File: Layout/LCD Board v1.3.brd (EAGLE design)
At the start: 37 parts, among them IC1 MAX3232CPE, IC2 MAX3232CPE, IC3 788TV, IC4 788TV

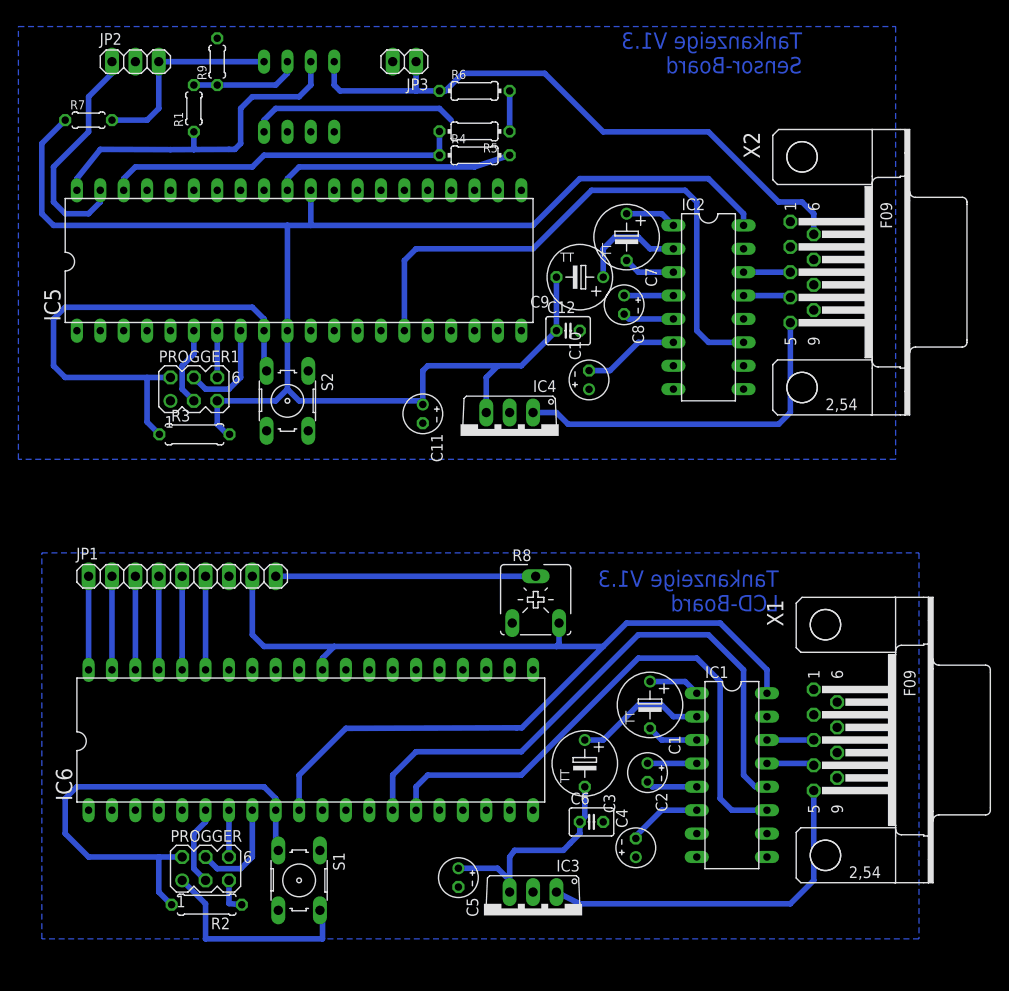
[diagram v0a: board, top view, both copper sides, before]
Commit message: Spannungsregler zu lm1117 und Input Cap hinzugefügt
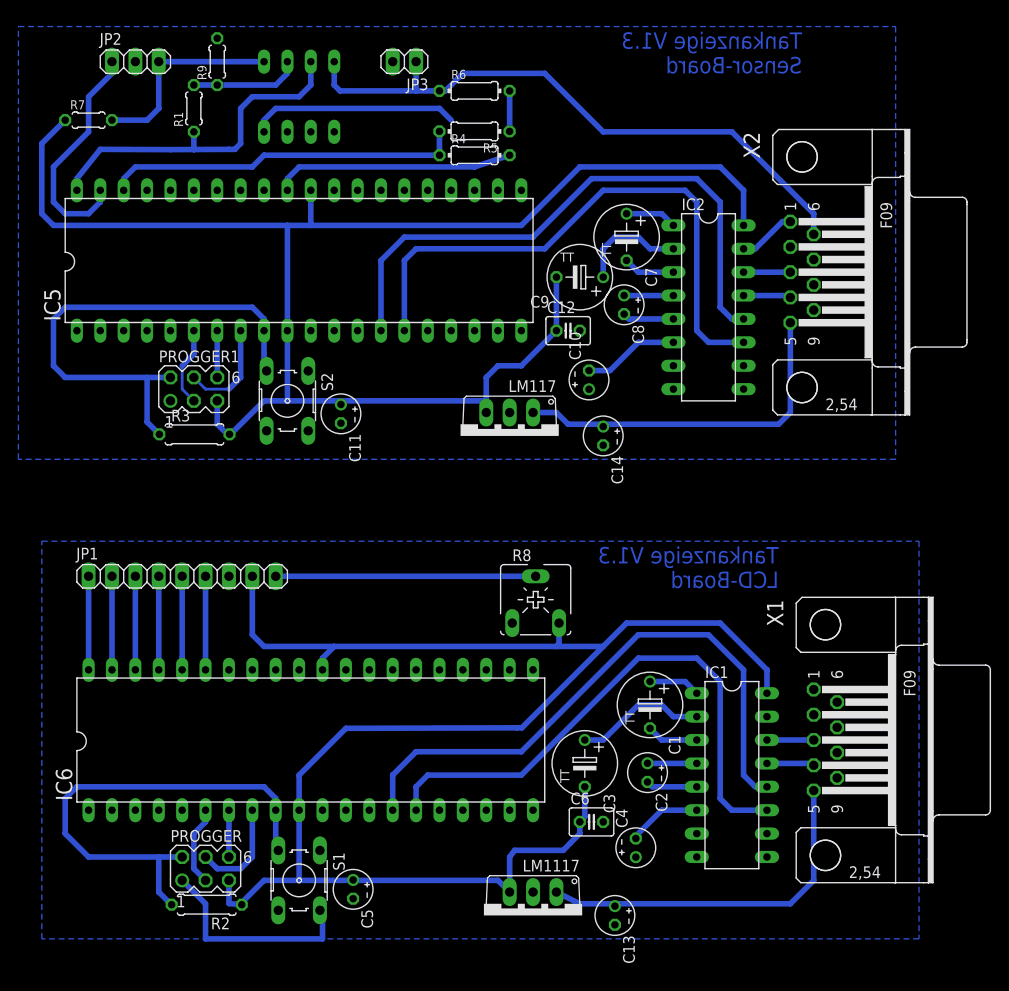
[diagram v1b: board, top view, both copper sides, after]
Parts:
- added C13, C14: 10uF, rcl:E2-4
- C11, C5: value 500uF -> 10uF
- moved C5 11.5 mm to (45.2, 6.65)
- moved C11 8.89 mm to (43.9, 58.3)
- renumbered IC3 to LM1117, IC4 to LM117
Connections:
- net +12V: now also C13.+, C14.+
- net GND: now also C13.-, C14.-
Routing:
- net N$33: track 0.00 -> 63.7 mm
- net VCC: track 318.4 -> 348.9 mm
- net GND: track 72.1 -> 78.4 mm
- net +12V: track 145.2 -> 145.7 mm

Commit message: Kleinere  Layoutchanges und Layouts zum Ausdrucken
Messplatine hinzugefüg
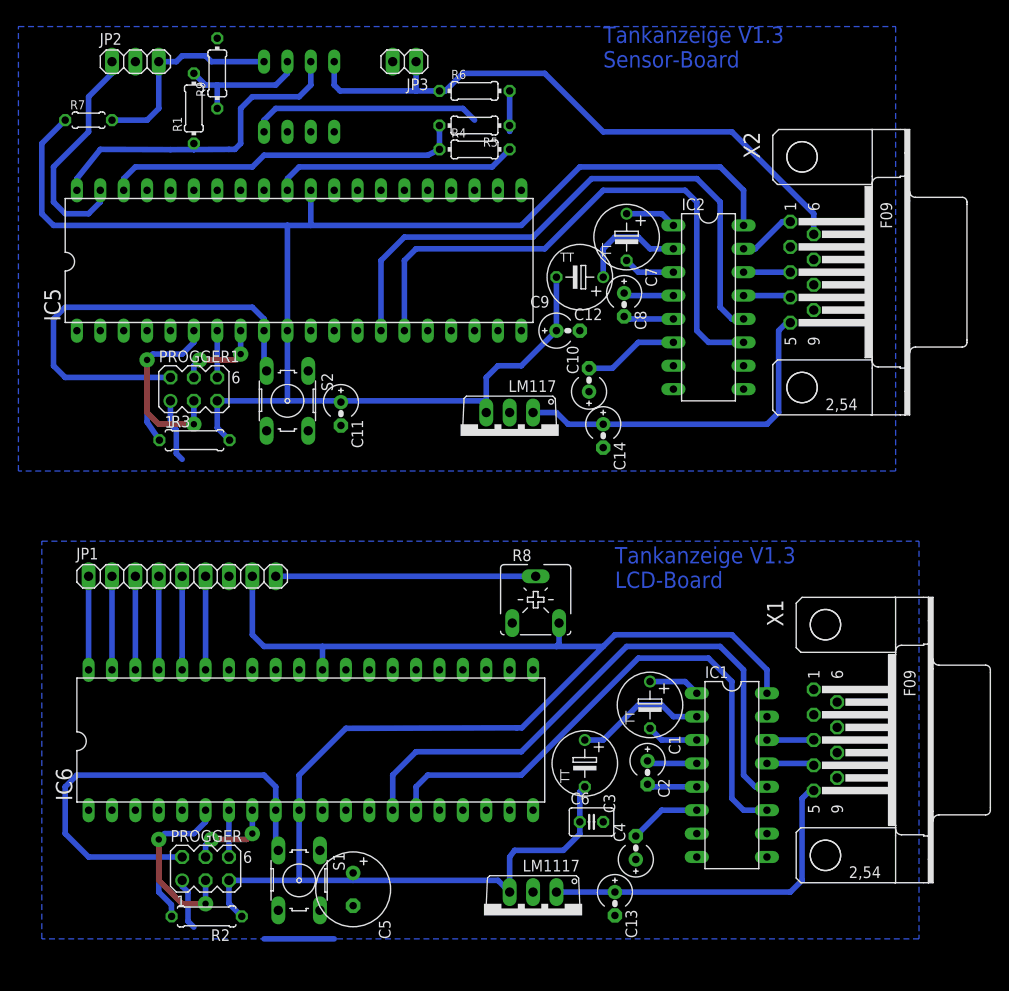
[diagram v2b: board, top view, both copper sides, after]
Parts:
- C10, C11, C13, C14, C2, C4, C8: device rcl:E2-4 -> rcl:E2,5RE
- C12: device rcl:C025-030X050 -> rcl:E2,5RE
- C5: device rcl:E2-4 -> rcl:E3,5-8
- R1, R9: device resistor:0204/5 -> rcl:0204/7
- moved C13 1.27 mm to (73.7, 5.08)
- moved R2 1.27 mm to (29.3, 3.71)
- moved R9 1.27 mm to (30.5, 95.2)
- moved R4 0.64 mm to (58.4, 87.0)
- moved R5 0.64 mm to (58.4, 89.6)
- moved R3 0.63 mm to (28.0, 55.4)
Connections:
- removed net GND: C10.+, C11.-, C12.2, C13.-, C14.-, C4.+, C5.-, C6.2, IC1.15, IC2.15, IC5.11, IC5.31, IC6.11, IC6.31, IC7.4, JP1.7, JP2.2, JP3.2, LM1117.2, LM117.2, PROGGER.1, PROGGER1.1, R4.2, R8.A, R9.2, S1.1, S1.2, S2.1, S2.2, X1.1, X2.1, X2.7
- new net $N4: C10.+, C11.-, C12.-, C13.-, C14.-, C4.+, C5.-, C6.2, IC1.15, IC2.15, IC5.11, IC5.31, IC6.11, IC6.31, IC7.4, JP1.7, JP2.2, JP3.2, LM1117.2, LM117.2, PROGGER.1, PROGGER1.1, R4.2, R8.A, R9.2, S1.1, S1.2, S2.1, S2.2, X1.1, X2.1, X2.7
- net VCC: now also C12.+; no longer C12.1
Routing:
- net GND: track 78.4 -> 0.00 mm
- net $N4: track 0.00 -> 78.3 mm
- net N$24: track 8.67 -> 21.0 mm, vias 0 -> 2
- net N$4: track 8.67 -> 20.3 mm, vias 0 -> 2
- net N$3: track 53.0 -> 58.1 mm
- net N$44: track 12.0 -> 15.0 mm
- net +12V: track 145.7 -> 143.3 mm
- net N$2: track 11.2 -> 9.42 mm, vias 0 -> 2
- net N$22: track 11.2 -> 9.42 mm, vias 0 -> 2
- net N$38: track 37.8 -> 36.5 mm
- net N$12: track 64.3 -> 63.2 mm
- net VCC: track 348.9 -> 349.8 mm
- net N$37: track 4.40 -> 5.02 mm
- net N$42: track 22.1 -> 22.6 mm
- added copper zone on layer 16, net $N4
- removed copper zone on layer 16, net GND
